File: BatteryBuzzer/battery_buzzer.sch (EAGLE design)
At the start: 30 parts, among them Q1 IRFML8244, Q2 IRFML8244, Q3 P-CHANNEL-MOSFETSOT23-3, Q4 P-CHANNEL-MOSFETSOT23-3, Q5 P-CHANNEL-MOSFETSOT23-3

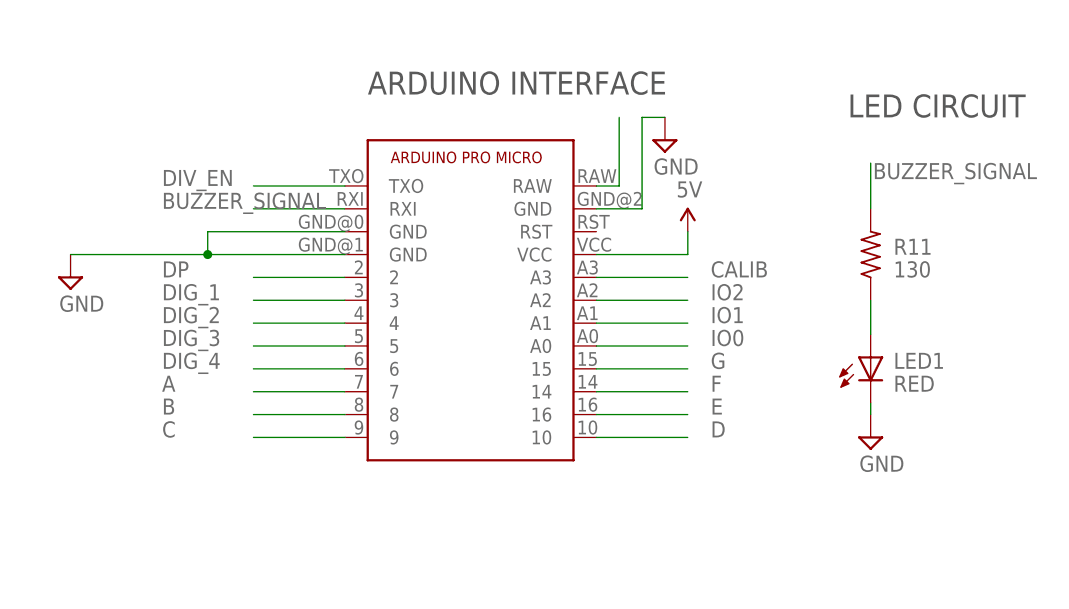
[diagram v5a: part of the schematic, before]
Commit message: switched some pin assignments
to make routing easier.
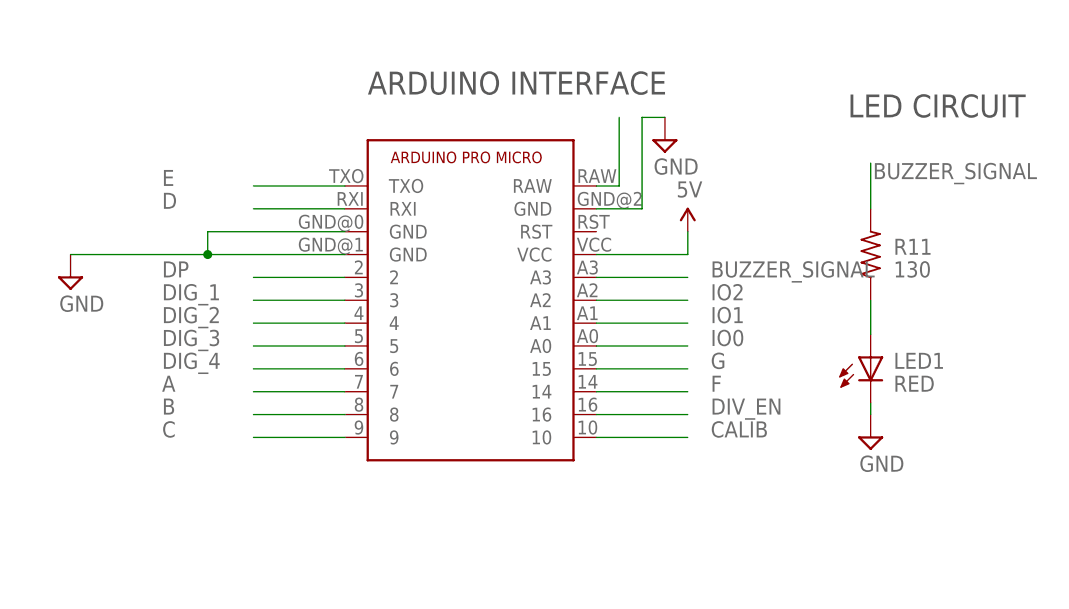
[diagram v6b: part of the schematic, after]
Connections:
- net BUZZER_SIGNAL: now also UC1.A3; no longer UC1.RXI
- net CALIB: now also UC1.10; no longer UC1.A3
- net D: now also UC1.RXI; no longer UC1.10
- net DIV_EN: now also UC1.16; no longer UC1.TXO
- net E: now also UC1.TXO; no longer UC1.16
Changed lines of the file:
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@@
 </segment>
 <segment>
-<pinref part="UC1" gate="G$1" pin="RXI"/>
-<wire x1="152.4" y1="73.66" x2="142.24" y2="73.66" width="0.1524" layer="91"/>
-<label x="132.08" y="73.66" size="1.778" layer="95"/>
+<pinref part="UC1" gate="G$1" pin="A3"/>
+<wire x1="180.34" y1="66.04" x2="190.5" y2="66.04" width="0.1524" layer="91"/>
+<label x="193.04" y="66.04" size="1.778" layer="95"/>
 </segment>
 </net>
@@
 </segment>
 <segment>
+<pinref part="UC1" gate="G$1" pin="16"/>
+<wire x1="180.34" y1="50.8" x2="190.5" y2="50.8" width="0.1524" layer="91"/>
+<label x="193.04" y="50.8" size="1.778" layer="95"/>
+</segment>
+</net>
+<net name="N$2" class="0">
+<segment>
+<pinref part="Q3" gate="G$1" pin="D"/>
+<pinref part="R2" gate="G$1" pin="2"/>
+<wire x1="129.54" y1="147.32" x2="129.54" y2="139.7" width="0.1524" layer="91"/>
+</segment>
+</net>
+<net name="N$3" class="0">
+<segment>
+<pinref part="Q4" gate="G$1" pin="D"/>
+<pinref part="R3" gate="G$1" pin="2"/>
+<wire x1="162.56" y1="147.32" x2="162.56" y2="139.7" width="0.1524" layer="91"/>
+</segment>
+</net>
+<net name="N$4" class="0">
+<segment>
+<pinref part="Q5" gate="G$1" pin="D"/>
+<pinref part="R4" gate="G$1" pin="2"/>
+<wire x1="195.58" y1="147.32" x2="195.58" y2="139.7" width="0.1524" layer="91"/>
+</segment>
+</net>
+<net name="DIG_1" class="0">
+<segment>
+<label x="58.42" y="60.96" size="1.778" layer="95"/>
+<pinref part="R14" gate="G$1" pin="2"/>
+<wire x1="55.88" y1="60.96" x2="58.42" y2="60.96" width="0.1524" layer="91"/>
+</segment>
+<segment>
+<pinref part="UC1" gate="G$1" pin="3"/>
+<wire x1="152.4" y1="63.5" x2="142.24" y2="63.5" width="0.1524" layer="91"/>
+<label x="132.08" y="63.5" size="1.778" layer="95"/>
+</segment>
+</net>
+<net name="D" class="0">
+<segment>
+<pinref part="DISP" gate="G$1" pin="3"/>
+<wire x1="43.18" y1="55.88" x2="50.8" y2="55.88" width="0.1524" layer="91"/>
+<label x="50.8" y="55.88" size="1.778" layer="95"/>
+</segment>
+<segment>
+<pinref part="UC1" gate="G$1" pin="RXI"/>
+<wire x1="152.4" y1="73.66" x2="142.24" y2="73.66" width="0.1524" layer="91"/>
+<label x="132.08" y="73.66" size="1.778" layer="95"/>
+</segment>
+</net>
+<net name="E" class="0">
+<segment>
+<pinref part="DISP" gate="G$1" pin="5"/>
+<wire x1="43.18" y1="50.8" x2="50.8" y2="50.8" width="0.1524" layer="91"/>
+<label x="50.8" y="50.8" size="1.778" layer="95"/>
+</segment>
+<segment>
 <pinref part="UC1" gate="G$1" pin="TXO"/>
 <wire x1="152.4" y1="76.2" x2="142.24" y2="76.2" width="0.1524" layer="91"/>
 <label x="132.08" y="76.2" size="1.778" layer="95"/>
-</segment>
-</net>
-<net name="N$2" class="0">
-<segment>
-<pinref part="Q3" gate="G$1" pin="D"/>
-<pinref part="R2" gate="G$1" pin="2"/>
-<wire x1="129.54" y1="147.32" x2="129.54" y2="139.7" width="0.1524" layer="91"/>
-</segment>
-</net>
-<net name="N$3" class="0">
-<segment>
-<pinref part="Q4" gate="G$1" pin="D"/>
-<pinref part="R3" gate="G$1" pin="2"/>
-<wire x1="162.56" y1="147.32" x2="162.56" y2="139.7" width="0.1524" layer="91"/>
-</segment>
-</net>
-<net name="N$4" class="0">
-<segment>
-<pinref part="Q5" gate="G$1" pin="D"/>
-<pinref part="R4" gate="G$1" pin="2"/>
-<wire x1="195.58" y1="147.32" x2="195.58" y2="139.7" width="0.1524" layer="91"/>
-</segment>
-</net>
-<net name="DIG_1" class="0">
-<segment>
-<label x="58.42" y="60.96" size="1.778" layer="95"/>
-<pinref part="R14" gate="G$1" pin="2"/>
-<wire x1="55.88" y1="60.96" x2="58.42" y2="60.96" width="0.1524" layer="91"/>
-</segment>
-<segment>
-<pinref part="UC1" gate="G$1" pin="3"/>
-<wire x1="152.4" y1="63.5" x2="142.24" y2="63.5" width="0.1524" layer="91"/>
-<label x="132.08" y="63.5" size="1.778" layer="95"/>
-</segment>
-</net>
-<net name="D" class="0">
-<segment>
-<pinref part="DISP" gate="G$1" pin="3"/>
-<wire x1="43.18" y1="55.88" x2="50.8" y2="55.88" width="0.1524" layer="91"/>
-<label x="50.8" y="55.88" size="1.778" layer="95"/>
-</segment>
-<segment>
-<pinref part="UC1" gate="G$1" pin="10"/>
-<wire x1="180.34" y1="48.26" x2="190.5" y2="48.26" width="0.1524" layer="91"/>
-<label x="193.04" y="48.26" size="1.778" layer="95"/>
-</segment>
-</net>
-<net name="E" class="0">
-<segment>
-<pinref part="DISP" gate="G$1" pin="5"/>
-<wire x1="43.18" y1="50.8" x2="50.8" y2="50.8" width="0.1524" layer="91"/>
-<label x="50.8" y="50.8" size="1.778" layer="95"/>
-</segment>
-<segment>
-<pinref part="UC1" gate="G$1" pin="16"/>
-<wire x1="180.34" y1="50.8" x2="190.5" y2="50.8" width="0.1524" layer="91"/>
-<label x="193.04" y="50.8" size="1.778" layer="95"/>
 </segment>
 </net>
@@
 </segment>
 <segment>
-<pinref part="UC1" gate="G$1" pin="A3"/>
-<wire x1="180.34" y1="66.04" x2="190.5" y2="66.04" width="0.1524" layer="91"/>
-<label x="193.04" y="66.04" size="1.778" layer="95"/>
-</segment>
-</net>
+<pinref part="UC1" gate="G$1" pin="10"/>
+<wire x1="180.34" y1="48.26" x2="190.5" y2="48.26" width="0.1524" layer="91"/>
+<label x="193.04" y="48.26" size="1.778" layer="95"/>
+</segment>
+</net>

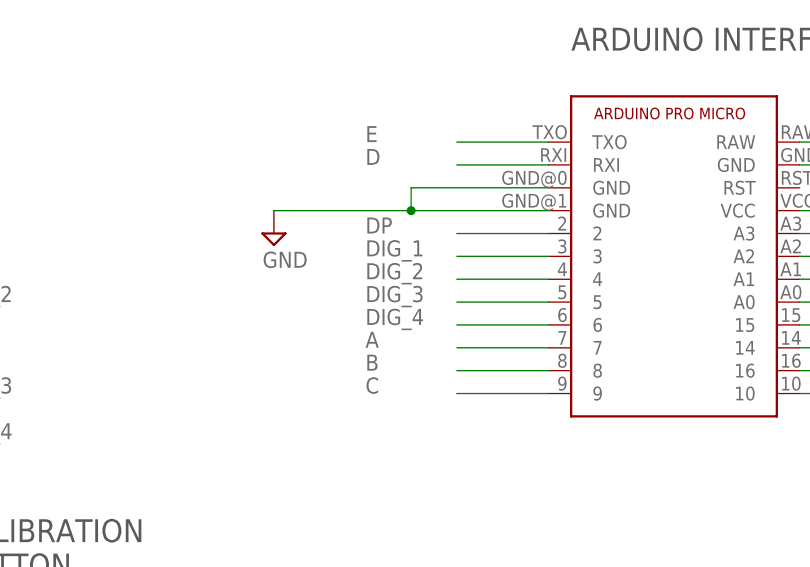
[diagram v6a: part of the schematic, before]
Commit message: more pin remapping.
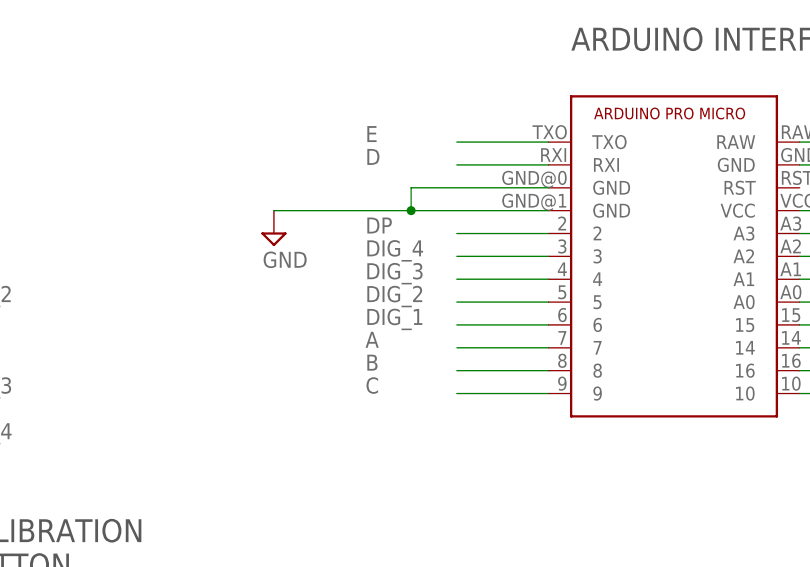
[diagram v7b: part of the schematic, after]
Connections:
- net DIG_1: now also UC1.6; no longer UC1.3
- net DIG_2: now also UC1.5; no longer UC1.4
- net DIG_3: now also UC1.4; no longer UC1.5
- net DIG_4: now also UC1.3; no longer UC1.6
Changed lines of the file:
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@@
 </segment>
 <segment>
-<pinref part="UC1" gate="G$1" pin="3"/>
-<wire x1="152.4" y1="63.5" x2="142.24" y2="63.5" width="0.1524" layer="91"/>
-<label x="132.08" y="63.5" size="1.778" layer="95"/>
+<pinref part="UC1" gate="G$1" pin="6"/>
+<wire x1="152.4" y1="55.88" x2="142.24" y2="55.88" width="0.1524" layer="91"/>
+<label x="132.08" y="55.88" size="1.778" layer="95"/>
 </segment>
 </net>
@@
 </segment>
 <segment>
-<pinref part="UC1" gate="G$1" pin="4"/>
-<wire x1="152.4" y1="60.96" x2="142.24" y2="60.96" width="0.1524" layer="91"/>
-<label x="132.08" y="60.96" size="1.778" layer="95"/>
+<pinref part="UC1" gate="G$1" pin="5"/>
+<wire x1="152.4" y1="58.42" x2="142.24" y2="58.42" width="0.1524" layer="91"/>
+<label x="132.08" y="58.42" size="1.778" layer="95"/>
 </segment>
 </net>
@@
 </segment>
 <segment>
-<pinref part="UC1" gate="G$1" pin="5"/>
-<wire x1="152.4" y1="58.42" x2="142.24" y2="58.42" width="0.1524" layer="91"/>
-<label x="132.08" y="58.42" size="1.778" layer="95"/>
+<pinref part="UC1" gate="G$1" pin="4"/>
+<wire x1="152.4" y1="60.96" x2="142.24" y2="60.96" width="0.1524" layer="91"/>
+<label x="132.08" y="60.96" size="1.778" layer="95"/>
 </segment>
 </net>
@@
 </segment>
 <segment>
-<pinref part="UC1" gate="G$1" pin="6"/>
-<wire x1="152.4" y1="55.88" x2="142.24" y2="55.88" width="0.1524" layer="91"/>
-<label x="132.08" y="55.88" size="1.778" layer="95"/>
+<pinref part="UC1" gate="G$1" pin="3"/>
+<wire x1="152.4" y1="63.5" x2="142.24" y2="63.5" width="0.1524" layer="91"/>
+<label x="132.08" y="63.5" size="1.778" layer="95"/>
 </segment>
 </net>

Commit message: and yet more pin remapping.
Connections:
- net D: now also UC1.2; no longer UC1.RXI
- net DP: now also UC1.TXO; no longer UC1.2
- net E: now also UC1.RXI; no longer UC1.TXO
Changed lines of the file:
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@@
 </segment>
 <segment>
-<pinref part="UC1" gate="G$1" pin="RXI"/>
-<wire x1="152.4" y1="73.66" x2="142.24" y2="73.66" width="0.1524" layer="91"/>
-<label x="132.08" y="73.66" size="1.778" layer="95"/>
+<pinref part="UC1" gate="G$1" pin="2"/>
+<wire x1="152.4" y1="66.04" x2="142.24" y2="66.04" width="0.1524" layer="91"/>
+<label x="132.08" y="66.04" size="1.778" layer="95"/>
 </segment>
 </net>
@@
 </segment>
 <segment>
-<pinref part="UC1" gate="G$1" pin="TXO"/>
-<wire x1="152.4" y1="76.2" x2="142.24" y2="76.2" width="0.1524" layer="91"/>
-<label x="132.08" y="76.2" size="1.778" layer="95"/>
+<pinref part="UC1" gate="G$1" pin="RXI"/>
+<wire x1="152.4" y1="73.66" x2="142.24" y2="73.66" width="0.1524" layer="91"/>
+<label x="132.08" y="73.66" size="1.778" layer="95"/>
 </segment>
 </net>
@@
 </segment>
 <segment>
-<pinref part="UC1" gate="G$1" pin="2"/>
-<wire x1="152.4" y1="66.04" x2="142.24" y2="66.04" width="0.1524" layer="91"/>
-<label x="132.08" y="66.04" size="1.778" layer="95"/>
+<pinref part="UC1" gate="G$1" pin="TXO"/>
+<wire x1="152.4" y1="76.2" x2="142.24" y2="76.2" width="0.1524" layer="91"/>
+<label x="132.08" y="76.2" size="1.778" layer="95"/>
 </segment>
 </net>
